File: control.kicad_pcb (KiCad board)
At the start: 4 copper layers, 60 x 35 mm, 76 parts, among them J101 Cortex_Debug, J102 JAE_DX07S016JA3, J103 WAGO-2065, J104 WAGO-2065, J201 2x05_Horizontal, J301 WAGO-2065, J302 WAGO-2065, J303 WAGO-2065, J401 SJ2-25504B-SMT-TR, SW101 SW_Push, SW102 SW_Push, U101 ATSAMD51G, U103 TPS78433QWDRBRQ1, U202 SN65MLVD203B, U301 74AHC1G125, U401 TLP2361, U501 TPSM33625, Y101 32k768

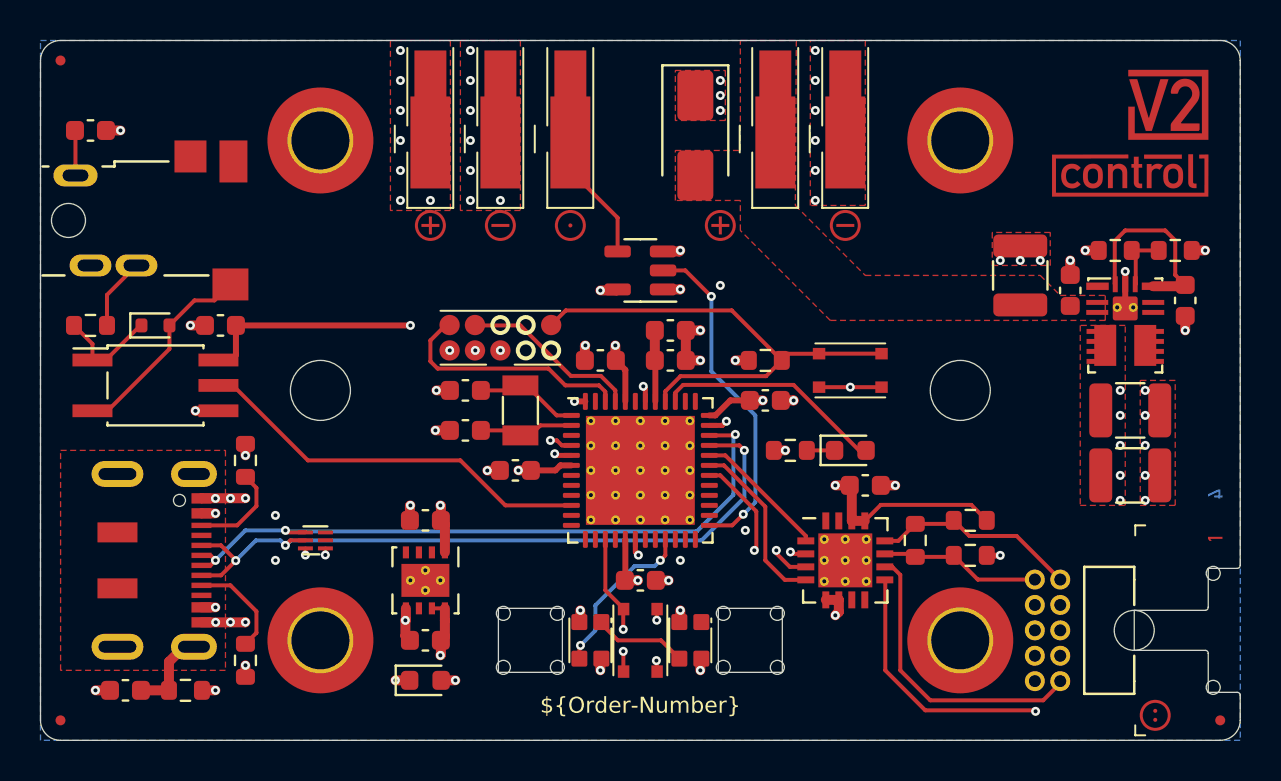
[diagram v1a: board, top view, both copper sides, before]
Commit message: Update DCDC
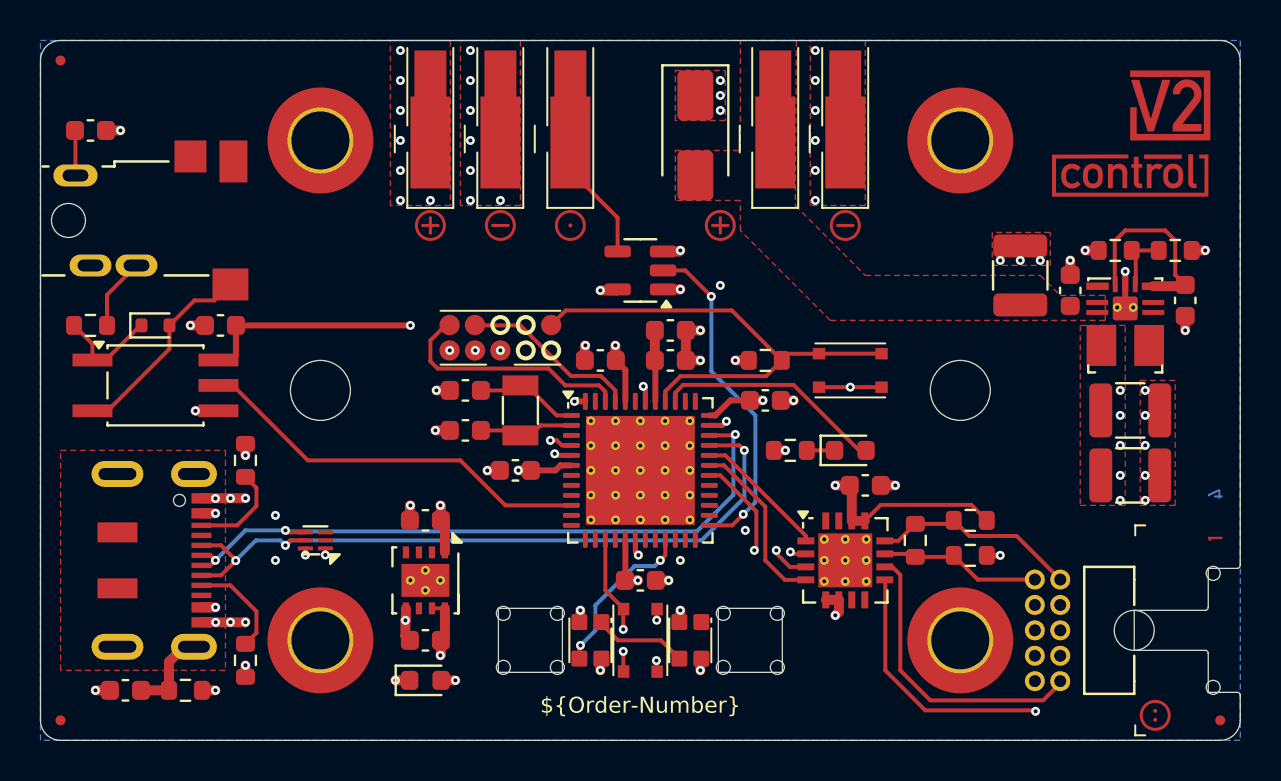
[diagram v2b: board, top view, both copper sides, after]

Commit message: Replace icons
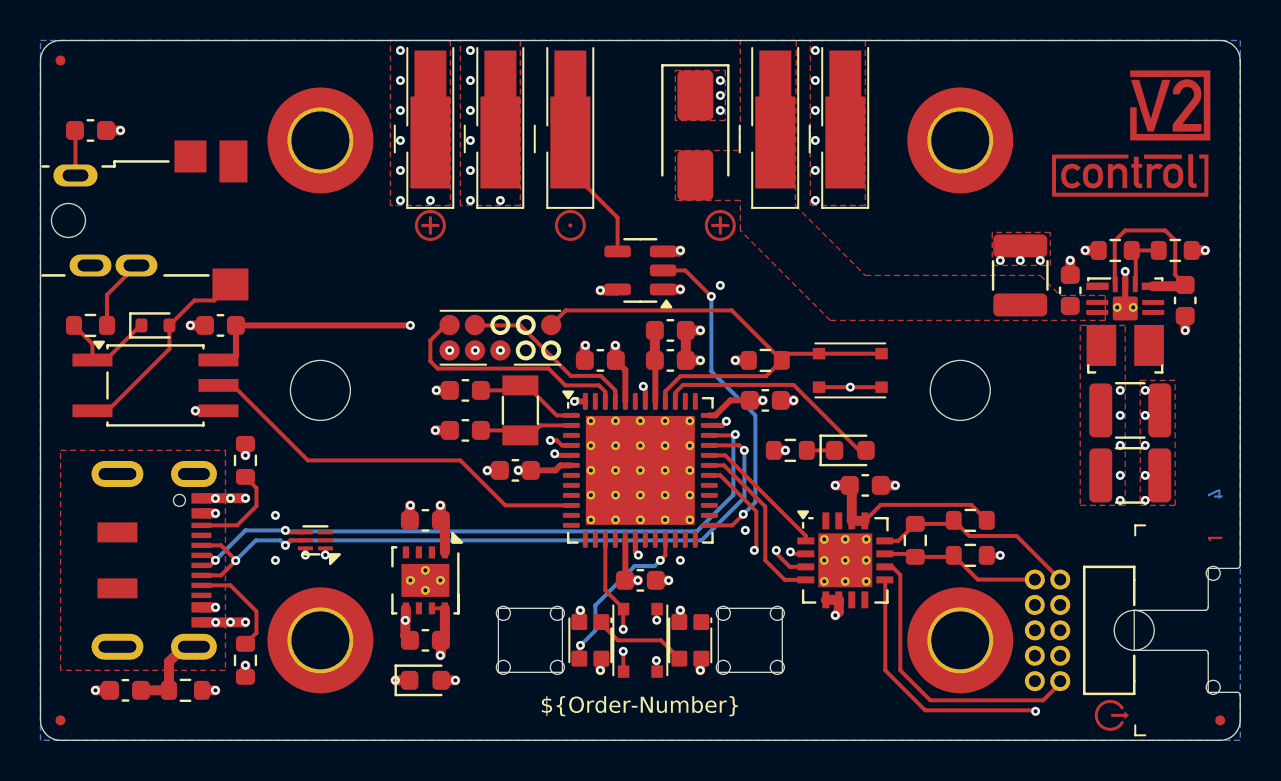
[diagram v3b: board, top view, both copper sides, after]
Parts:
- removed ICON103, ICON105: Minus, V2_Artwork:Minus_Small
- ICON107: value Socket -> Arrow_Out; footprint V2_Artwork:Socket_Small -> V2_Artwork:Arrow_Out
- U103: value TPS78433QWDRBRQ1 -> TPS78433QWDRBRQ1
- moved ICON107 2.25 mm to (170.5, 113.8)
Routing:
- net unconnected-(J102-VBUS-PadV)_0: track 6.72 -> 0.00 mm, vias 2 -> 0
- net unconnected-(J102-VBUS-PadV): track 0.00 -> 6.72 mm, vias 0 -> 2

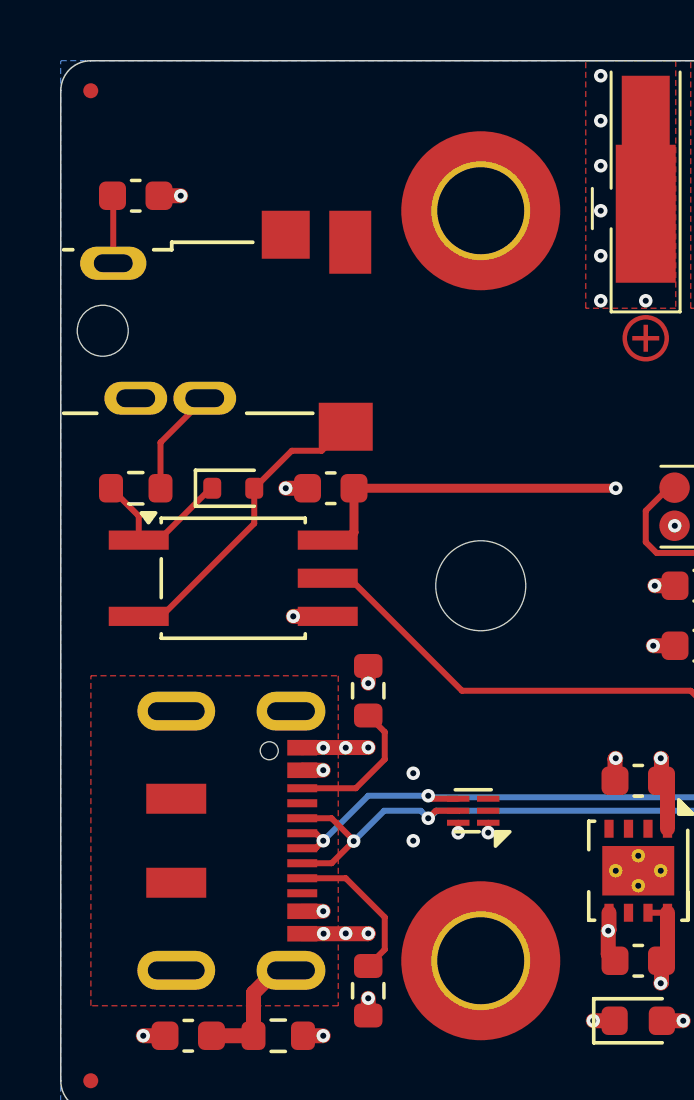
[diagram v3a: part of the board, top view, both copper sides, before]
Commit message: Update TRS socket
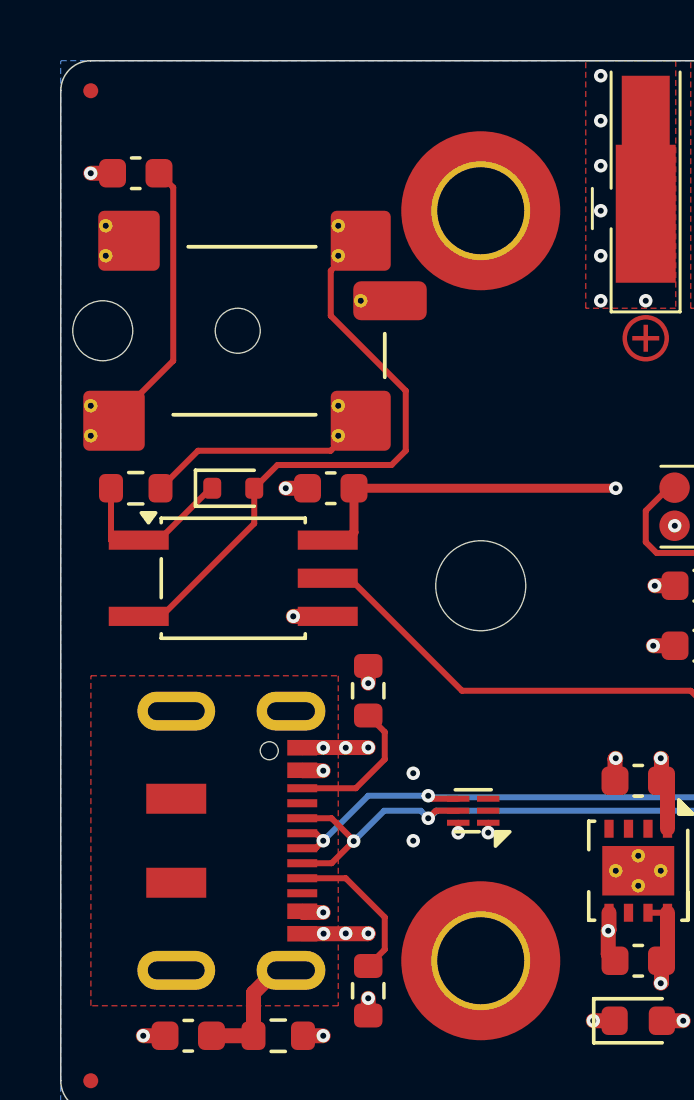
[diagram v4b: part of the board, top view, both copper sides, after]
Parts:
- J401: value SJ2-25504B-SMT-TR -> SJ2-25404B-SMT-TR; footprint V2_Connector_Audio:CUI_SJ2-25504B-SMT-TR -> V2_Connector_Audio:CUI_SJ2-25404B-SMT-TR
- moved C401 0.75 mm to (119.5, 83.8), turned to 180 degrees
- moved J401 0.25 mm to (122.5, 89.0)
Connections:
- net Net-(J401-S) renamed /MIDI In/Sleeve
- J102 pad V: unconnected-(J102-VBUS-PadV)_0 -> VBUS
- J401 pad 2: unconnected-(J401-T-Pad2) -> /MIDI In/Tip
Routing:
- net /MIDI In/Tip: track 10.2 -> 20.3 mm
- net /MIDI In/Sleeve: track 2.26 -> 9.26 mm
- net unconnected-(J102-VBUS-PadV): track 6.72 -> 0.00 mm, vias 2 -> 0
- net VBUS: track 0.00 -> 6.60 mm, vias 0 -> 2
- net /MIDI In/Ring: track 3.61 -> 7.61 mm
- net Net-(D401-K): track 5.28 -> 5.82 mm

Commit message: Refresh
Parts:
- removed the C104 at (148.5, 96.0)
- removed R202, R203: 10k, Resistor_SMD:R_0603_1608Metric
- U201: renamed from U202; value SN65MLVD203B -> THVD24x2; footprint V2_Package_DFN_QFN:WQFN-16-1EP_4x4mm_P0.65mm_EP2.7x2.7mm_ThermalVias -> V2_Package_SON:VSON-10-4-1EP_3x3mm_P0.5mm_EP1.65x2.4mm_ThermalVias
- U401: footprint Package_SO:SO-5_4.4x3.6mm_P1.27mm -> Package_SO:SO-5-6_4.55x3.7mm_P1.27mm
- moved ICON101 3.04 mm to (173.5, 113.2)
- moved C101 1.50 mm to (148.5, 96.0)
- moved U201 0.79 mm to (157.5, 105.2)
- moved C201 0.75 mm to (157.5, 102.2), turned to 180 degrees
- moved ICON102 0.25 mm to (136.5, 89.5)
- moved ICON104 0.25 mm to (150.8, 89.2)
- moved ICON106 0.25 mm to (143.5, 89.5)
- moved R201 0.25 mm to (161.0, 105.0)
- moved TVS101 0.25 mm to (136.2, 111.8)
- renumbered C103 to C101, C105 to C102, C106 to C103, C107 to C104, C108 to C105, C110 to C106, C109 to C107, C101 to C108, C102 to C109, C111 to C110, C402 to C401, C401 to C402, C505 to C503, C503 to C504, C504 to C505, D102 to D101, D103 to D102, D101 to D103, ICON107 to ICON101, ICON104 to ICON102, ICON102 to ICON103, ICON106 to ICON104, ICON101 to ICON105, ICON108 to ICON106, INFO102 to INFO101, INFO101 to INFO102, R102 to R101, R105 to R102, R101 to R105, SW102 to SW101, SW101 to SW102, U103 to U101, U101 to U102
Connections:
- U201 pad 10: /Link Socket/TX-Z -> +3V3
- U201 pad 11: /Link Socket/RX-B -> GND
- U201 pad 6: GND -> /Link Socket/TX-Y
- U201 pad 7: unconnected-(U202-Pad7) -> /Link Socket/TX-Z
- U201 pad 8: unconnected-(U202-Pad8) -> /Link Socket/RX-B
- U201 pad 9: /Link Socket/TX-Y -> /Link Socket/RX-A
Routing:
- net +3V3: track 36.9 -> 27.9 mm, vias 10 -> 11
- net +5V: track 6.84 -> 3.40 mm
- net GND: track 38.8 -> 35.8 mm, vias 77 -> 71
- net /VDDCORE: track 3.56 -> 2.06 mm
- net /Socket-TX-Enable: track 8.09 -> 7.02 mm
- net /Socket-TX: track 8.77 -> 7.73 mm
- net /Link Socket/TX-Y: track 14.4 -> 15.4 mm
- net /Link Socket/RX-B: track 8.11 -> 8.94 mm
- net /Link Socket/TX-Z: track 14.8 -> 15.6 mm
- net VBUS: track 6.60 -> 7.15 mm
- net /RESET: track 25.0 -> 24.4 mm
- added copper zone on F.Cu, net +3V3
- added copper zone on In2.Cu, net GND
